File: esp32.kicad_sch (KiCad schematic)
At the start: 14 parts, among them IC1 ESP32-S3-WROOM-1, J10 Conn_01x07_Socket, J99 Conn_ARM_JTAG_SWD_20, Q3 2N7002

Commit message: add gitignore
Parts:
- C10: value 100nF / 50V -> 100nF / 50V
- renumbered J10 to J98, R7 to R6, R6 to R7

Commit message: Adapted gitignore Add LAN Add USB2RS232
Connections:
- net MISO renamed RFID_MISO
- net MOSI renamed RFID_MOSI
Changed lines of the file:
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@@
 		)
 	)
-	(global_label "MISO"
+	(global_label "RFID_MISO"
 		(shape output)
 		(at 162.56 82.55 0)
@@
 		)
 		(property "Intersheetrefs" "${INTERSHEET_REFS}"
-			(at 170.062 82.55 0)
+			(at 175.3424 82.55 0)
 			(hide yes)
 			(show_name no)
@@
 		)
 	)
-	(global_label "MOSI"
+	(global_label "RFID_MOSI"
 		(shape output)
 		(at 162.56 77.47 0)
@@
 		)
 		(property "Intersheetrefs" "${INTERSHEET_REFS}"
-			(at 170.062 77.47 0)
+			(at 175.3424 77.47 0)
 			(hide yes)
 			(show_name no)

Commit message: Connect W5500 to ESP32, fix RFID SCK, add relay flyback diode
- ESP32: add global labels LAN_CS/RST/INT/SCK/MISO/MOSI on GPIO 5/6/7/14/15/16
  (matches WIRING_OVERVIEW.md)
- ESP32: rename SCK label to RFID_SCK so GPIO12 reaches PN532 connector J1
- ESP32: connect WAKE_UP (optocoupler U3) to GPIO21
- LAN: power WIZ850io from +3.3V instead of unconnected +3V3 net
- Interfaces: add flyback diode D5 (1N4148W, LCSC C81598) across K1 coil
- Interfaces: tie R12 pull-up to +3.3V, set value to 10k
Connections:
- net LAN_SCK: now reaches IC1.22 (GPIO14/TOUCH14/ADC2_CH3/FSPIWP/FSPIDQS/SUBSPIWP)
- net WAKE_UP: now reaches IC1.23 (GPIO21)
- net LAN_CS: now reaches IC1.5 (GPIO5/TOUCH5/ADC1_CH4)
- net LAN_RST: now reaches IC1.6 (GPIO6/TOUCH6/ADC1_CH5)
- net LAN_INT: now reaches IC1.7 (GPIO7/TOUCH7/ADC1_CH6)
- net LAN_MISO: now reaches IC1.8 (GPIO15/U0RTS/ADC2_CH4/XTAL_32K_P)
- net LAN_MOSI: now reaches IC1.9 (GPIO16/U0CTS/ADC2_CH5/XTAL_32K_N)
- net SCK renamed RFID_SCK
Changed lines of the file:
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@@
+	(wire
+		(pts
+			(xy 157.48 67.31) (xy 171.45 67.31)
+		)
+		(stroke
+			(width 0)
+			(type default)
+		)
+	)
 	(wire
 		(pts
@@
 	(wire
 		(pts
+			(xy 54.61 44.45) (xy 66.04 44.45)
+		)
+		(stroke
+			(width 0)
+			(type default)
+		)
+	)
+	(wire
+		(pts
 			(xy 157.48 36.83) (xy 163.83 36.83)
 		)
@@
 	(wire
 		(pts
+			(xy 54.61 41.91) (xy 66.04 41.91)
+		)
+		(stroke
+			(width 0)
+			(type default)
+		)
+	)
+	(wire
+		(pts
 			(xy 157.48 72.39) (xy 187.96 72.39)
 		)
@@
 	(wire
 		(pts
+			(xy 157.48 92.71) (xy 171.45 92.71)
+		)
+		(stroke
+			(width 0)
+			(type default)
+		)
+	)
+	(wire
+		(pts
 			(xy 34.29 30.48) (xy 49.53 30.48)
 		)
@@
 	(wire
 		(pts
+			(xy 157.48 64.77) (xy 162.56 64.77)
+		)
+		(stroke
+			(width 0)
+			(type default)
+		)
+	)
+	(wire
+		(pts
 			(xy 233.68 46.99) (xy 245.11 46.99)
 		)
@@
 	(wire
 		(pts
+			(xy 157.48 62.23) (xy 171.45 62.23)
+		)
+		(stroke
+			(width 0)
+			(type default)
+		)
+	)
+	(wire
+		(pts
 			(xy 157.48 74.93) (xy 171.45 74.93)
 		)
@@
 		(pts
 			(xy 69.85 168.91) (xy 85.09 168.91)
+		)
+		(stroke
+			(width 0)
+			(type default)
+		)
+	)
+	(wire
+		(pts
+			(xy 157.48 85.09) (xy 171.45 85.09)
 		)
 		(stroke
@@
 		)
 	)
+	(global_label "WAKE_UP"
+		(shape output)
+		(at 171.45 92.71 0)
+		(fields_autoplaced yes)
+		(effects
+			(font
+				(size 1.27 1.27)
+			)
+			(justify left)
+		)
+		(property "Intersheetrefs" "${INTERSHEET_REFS}"
+			(at 182.9623 92.71 0)
+			(hide yes)
+			(show_name no)
+			(do_not_autoplace no)
+			(effects
+				(font
+					(size 1.27 1.27)
+				)
+				(justify left)
+			)
+		)
+	)
 	(global_label "IO_PUMP_RELAIS"
 		(shape input)
@@
 		)
 	)
+	(global_label "LAN_MOSI"
+		(shape output)
+		(at 54.61 44.45 180)
+		(fields_autoplaced yes)
+		(effects
+			(font
+				(size 1.27 1.27)
+			)
+			(justify right)
+		)
+		(property "Intersheetrefs" "${INTERSHEET_REFS}"
+			(at 42.6138 44.45 0)
+			(hide yes)
+			(show_name no)
+			(do_not_autoplace no)
+			(effects
+				(font
+					(size 1.27 1.27)
+				)
+				(justify right)
+			)
+		)
+	)
 	(global_label "RFID_SS"
 		(shape output)
@@
 		)
 	)
+	(global_label "LAN_MISO"
+		(shape output)
+		(at 54.61 41.91 180)
+		(fields_autoplaced yes)
+		(effects
+			(font
+				(size 1.27 1.27)
+			)
+			(justify right)
+		)
+		(property "Intersheetrefs" "${INTERSHEET_REFS}"
+			(at 42.6138 41.91 0)
+			(hide yes)
+			(show_name no)
+			(do_not_autoplace no)
+			(effects
+				(font
+					(size 1.27 1.27)
+				)
+				(justify right)
+			)
+		)
+	)
 	(global_label "RFID_MISO"
 		(shape output)
@@
 				)
 				(justify right)
+			)
+		)
+	)
+	(global_label "LAN_RST"
+		(shape output)
+		(at 162.56 64.77 0)
+		(fields_autoplaced yes)
+		(effects
+			(font
+				(size 1.27 1.27)
+			)
+			(justify left)
+		)
+		(property "Intersheetrefs" "${INTERSHEET_REFS}"
+			(at 173.4071 64.77 0)
+			(hide yes)
+			(show_name no)
+			(do_not_autoplace no)
+			(effects
+				(font
+					(size 1.27 1.27)
+				)
+				(justify left)
 			)
 		)
@@
 		)
 	)
+	(global_label "LAN_SCK"
+		(shape output)
+		(at 171.45 85.09 0)
+		(fields_autoplaced yes)
+		(effects
+			(font
+				(size 1.27 1.27)
+			)
+			(justify left)
+		)
+		(property "Intersheetrefs" "${INTERSHEET_REFS}"
+			(at 182.5995 85.09 0)
+			(hide yes)
+			(show_name no)
+			(do_not_autoplace no)
+			(effects
+				(font
+					(size 1.27 1.27)
+				)
+				(justify left)
+			)
+		)
+	)
 	(global_label "TCK"
 		(shape output)
@@
 		)
 	)
-	(global_label "SCK"
+	(global_label "RFID_SCK"
 		(shape output)
 		(at 171.45 80.01 0)
@@
 		)
 		(property "Intersheetrefs" "${INTERSHEET_REFS}"
-			(at 178.1053 80.01 0)
+			(at 183.3857 80.01 0)
 			(hide yes)
 			(show_name no)
@@
 		)
 	)
+	(global_label "LAN_CS"
+		(shape output)
+		(at 171.45 62.23 0)
+		(fields_autoplaced yes)
+		(effects
+			(font
+				(size 1.27 1.27)
+			)
+			(justify left)
+		)
+		(property "Intersheetrefs" "${INTERSHEET_REFS}"
+			(at 181.3295 62.23 0)
+			(hide yes)
+			(show_name no)
+			(do_not_autoplace no)
+			(effects
+				(font
+					(size 1.27 1.27)
+				)
+				(justify left)
+			)
+		)
+	)
 	(global_label "TDO"
 		(shape output)
@@
 			)
 		)
+	)
+	(global_label "LAN_INT"
+		(shape output)
+		(at 171.45 67.31 0)
+		(fields_autoplaced yes)
+		(effects
+			(font
+				(size 1.27 1.27)
+			)
+			(justify left)
+		)
+		(property "Intersheetrefs" "${INTERSHEET_REFS}"
+			(at 181.7529 67.31 0)
+			(hide yes)
+			(show_name no)
+			(do_not_autoplace no)
+			(effects
+				(font
+					(size 1.27 1.27)
+				)
+				(justify left)
+			)
+		)

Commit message: Add input protection, fix USB-C/CP2102 supply, harden optocoupler input
Power supply:
- Add 12V input protection: PTC fuse F1 (1.1A/33V, C70119), TVS D6
  (SMAJ15CA, C151939), reverse polarity Schottky D7 (SS34, C8678) and
  bulk cap C13 (100uF/25V, C179802)

USB2RS232:
- Power CP2102N (VDD/REGIN) from +3.3V via R25 (0R)
- Add 5k1 pull-downs R23/R24 on USB-C CC1/CC2 so C-to-C hosts supply VBUS

ESP32 / Interfaces:
- Add 100k gate pull-downs R26/R27/R28 on Q2/Q1/Q3 (relay, LED, buzzer
  stay off during reset/boot)
- Buzzer flyback D1: 1N4148W SOD-123 (C81598) instead of undefined SOT-23
- WAKE_UP input (J8/U3): series zener D8 (BZT52C6V8, C173404), reverse
  polarity diode D9 (1N4148W), R11 = 1k5 0805 (C4310); switches at ~9V,
  safe up to 14.4V
- IC1 value set to ESP32-S3-WROOM-1U to match footprint
- Add no-connect flags on unused ESP32, J99 and K1 pins
- Remove duplicate local labels IO_PUMP_LED/IO_PUMP_RELAIS
- Move off-grid symbols, labels and wires onto grid

PCB: update from schematic
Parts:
- added R28: 100k, Resistor_SMD:R_0402_1005Metric_Pad0.72x0.64mm_HandSolder, symbol Device:R
- D1: value D -> 1N4148W; footprint Package_TO_SOT_SMD:SOT-23 -> Diode_SMD:D_SOD-123; LCSC (none) -> C81598
- IC1: value ESP32-S3-WROOM-1 -> ESP32-S3-WROOM-1U
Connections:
- net GND: now also R28.2
- net at Q3.1 (G), R6.1: now also R28.1
- no-connect marks 0 -> 15

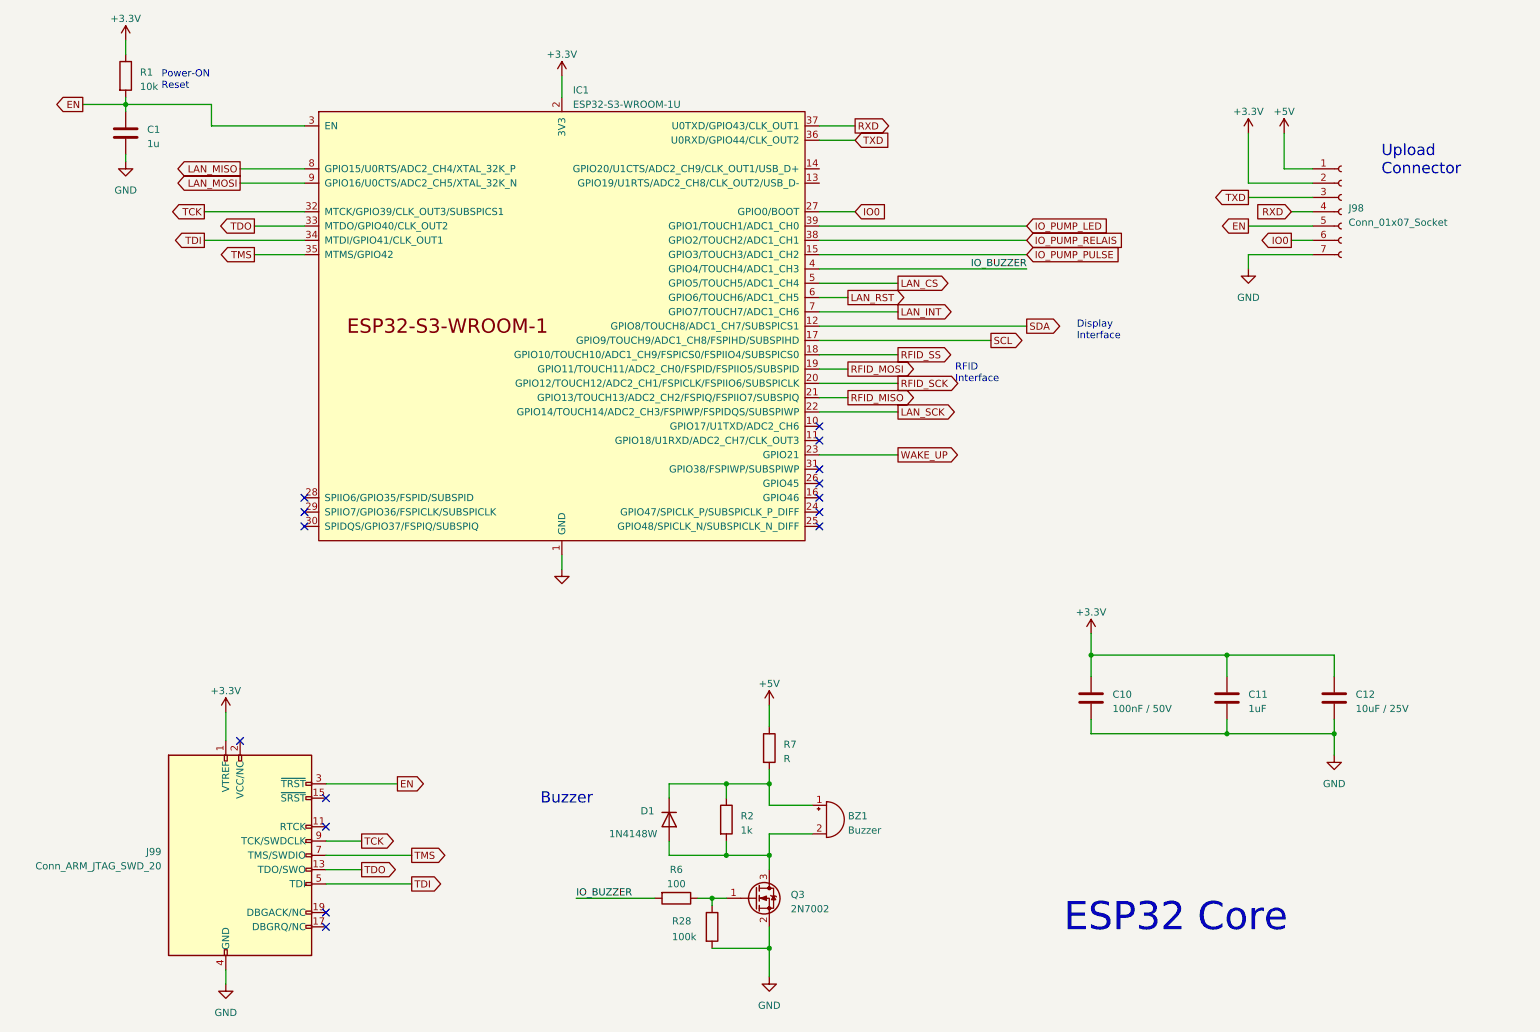
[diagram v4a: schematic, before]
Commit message: Add native ESP32-S3 USB port, move buzzer driver to Interfaces sheet
ESP32:
- Add USB-C J4 for ESP32-S3 native USB (USB-Serial-JTAG):
  D+ -> GPIO20, D- -> GPIO19 via 0R series resistors R31/R32 (0402, C17168),
  ESD diodes D10/D12 (LESD5D5.0CT1G), CC pull-downs R29/R30 5k1,
  VBUS not connected (no-connect flag)
- Move JTAG header J99 and decoupling C10-C12 to free space for J4

Interfaces:
- Move buzzer driver (Q3, R6, R28, R2, R7, D1, BZ1) from ESP32 sheet
- Make IO_BUZZER a global label so GPIO4 still reaches R6/Q3
- Shift optocoupler input block (J8, D8, D9, R11, R12, U3) down

Power supply:
- Add PWR_FLAG on +12V after reverse polarity diode D7 (ERC clean)

PCB: update from schematic
ERC: 0 errors, 5 warnings (2N7002 symbol lib mismatch, unused RFID_IRQ/RST)
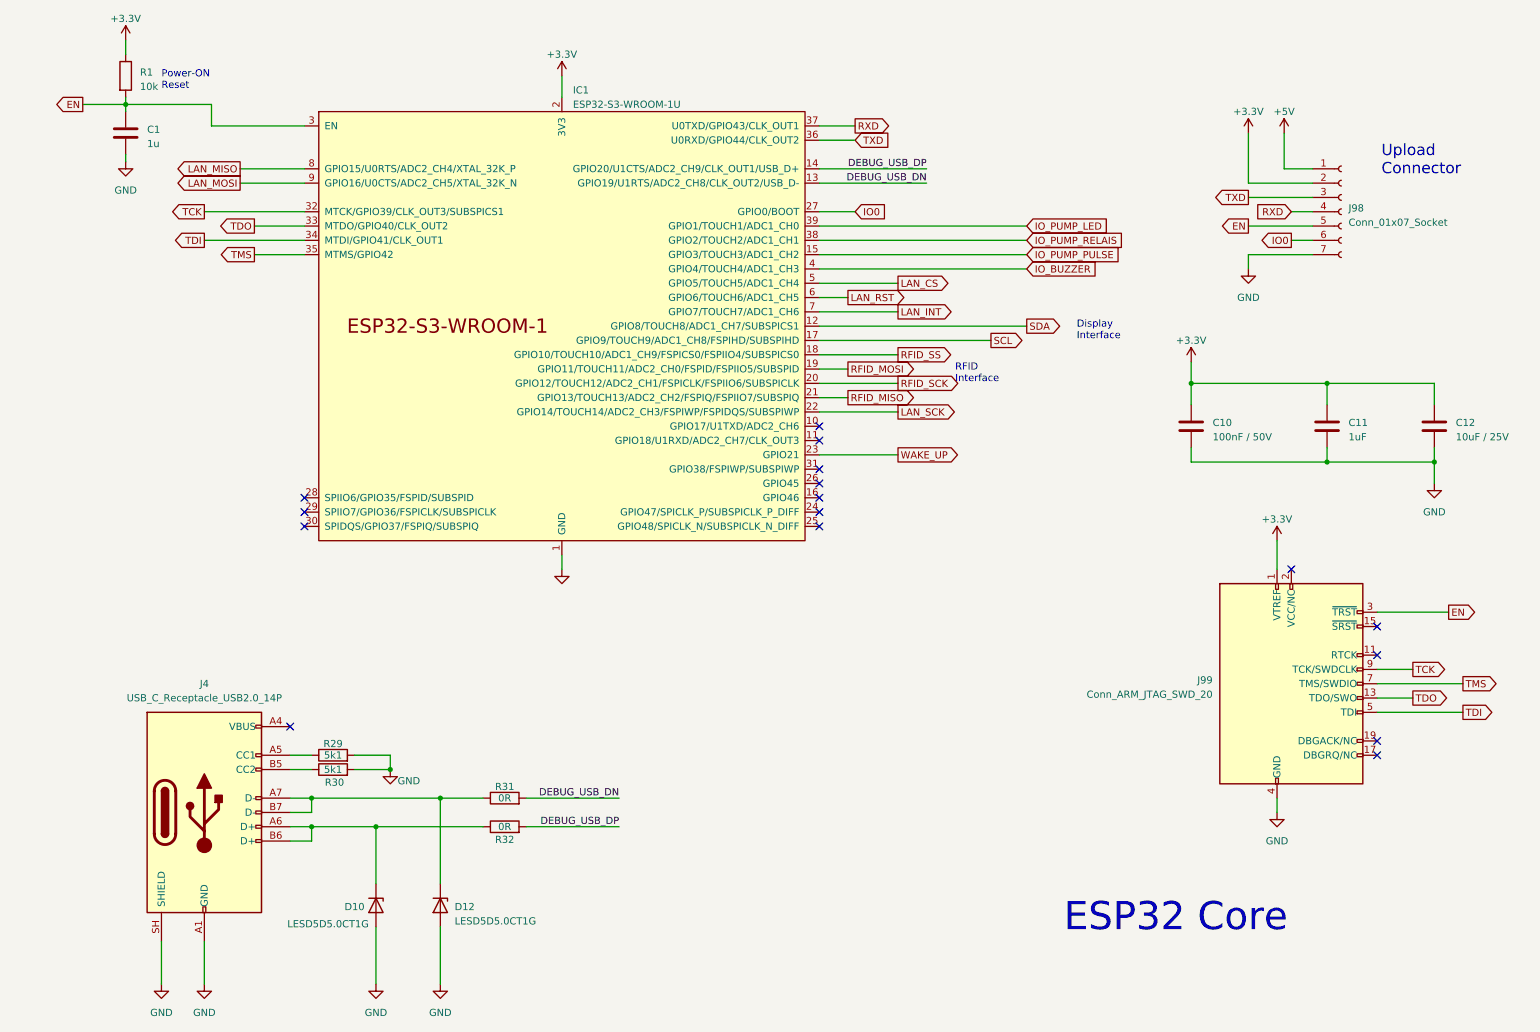
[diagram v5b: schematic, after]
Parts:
- removed BZ1: Buzzer, GA_Fuelstation_Terminal:8530-SMD, symbol Device:Buzzer
- removed D1: 1N4148W, Diode_SMD:D_SOD-123, symbol Device:D
- removed Q3: 2N7002, Package_TO_SOT_SMD:SOT-23, symbol Transistor_FET:2N7002
- removed R2: 1k, Resistor_SMD:R_0805_2012Metric_Pad1.20x1.40mm_HandSolder, symbol Device:R
- removed R28: 100k, Resistor_SMD:R_0402_1005Metric_Pad0.72x0.64mm_HandSolder, symbol Device:R
- removed R6: 100, Resistor_SMD:R_0805_2012Metric_Pad1.20x1.40mm_HandSolder, symbol Device:R
- removed R7: R, Resistor_SMD:R_0805_2012Metric_Pad1.20x1.40mm_HandSolder, symbol Device:R
- added D10, D12: LESD5D5.0CT1G, Diode_SMD:D_SOD-523, symbol Diode:ESD5Zxx
- added J4: USB_C_Receptacle_USB2.0_14P, Connector_USB:USB_C_Receptacle_HRO_TYPE-C-31-M-12, symbol Connector:USB_C_Receptacle_USB2.0_14P
- added R29, R30: 5k1, Resistor_SMD:R_0603_1608Metric_Pad0.98x0.95mm_HandSolder, symbol Device:R
- added R31, R32: 0R, Resistor_SMD:R_0402_1005Metric, symbol Device:R
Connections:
- net GND: now also D10.2 (A), D12.2 (A), J4.A1 (GND), J4.A12 (GND), J4.B1 (GND), J4.B12 (GND), J4.SH (SHIELD), R29.2, R30.2
- net DEBUG_USB_DN: now reaches IC1.13 (GPIO19/U1RTS/ADC2_CH8/CLK_OUT2/USB_D-)
- net DEBUG_USB_DN: now also R31.2
- net DEBUG_USB_DP: now reaches IC1.14 (GPIO20/U1CTS/ADC2_CH9/CLK_OUT1/USB_D+)
- net DEBUG_USB_DP: now also R32.2
- new net: J4.A4 (VBUS), J4.A9 (VBUS), J4.B4 (VBUS), J4.B9 (VBUS)
- new net: J4.A5 (CC1), R29.1
- new net: D10.1 (K), J4.A6 (D+), J4.B6 (D+), R32.1
- new net: D12.1 (K), J4.A7 (D-), J4.B7 (D-), R31.1
- new net: J4.B5 (CC2), R30.1
- no-connect marks 15 -> 16
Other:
- note removed: "Buzzer"
- moved on the sheet: C10, C11, C12, J99
